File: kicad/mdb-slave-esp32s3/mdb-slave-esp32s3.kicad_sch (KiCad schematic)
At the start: 44 parts, among them J1 MDB_Connector, J2 USB_C_Receptacle_USB2.0_16P, J3 Conn_01x03_Pin, J8 Conn_01x04_Pin, Q7 MMBT3904, SW1 SW_Push, U1 TLP785, U3 ESP32-S3FH4R2, U4 TLP785, U5 LM2594HVM-3.3, Y1 Crystal_GND24

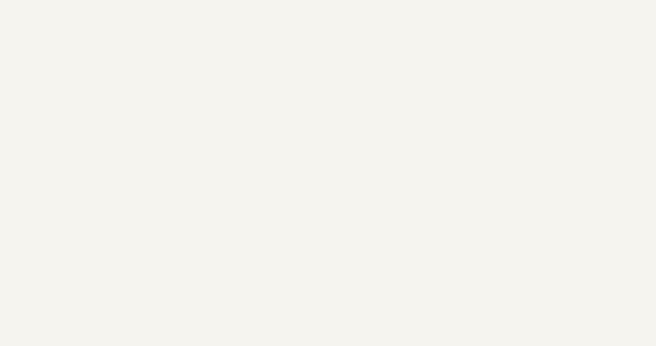
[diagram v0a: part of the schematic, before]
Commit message: small mounting hole
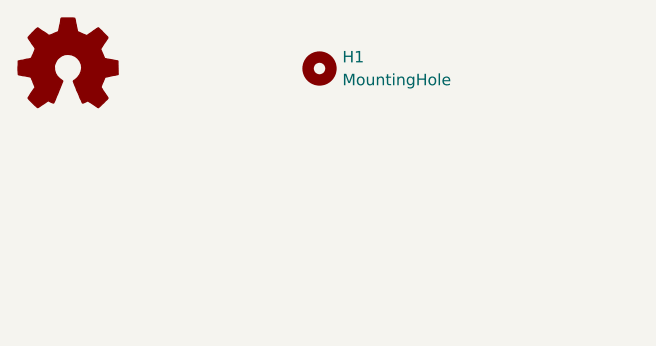
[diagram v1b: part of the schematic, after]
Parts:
- added H1: MountingHole, MountingHole:MountingHole_2.1mm, symbol Mechanical:MountingHole
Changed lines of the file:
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@@
+	)
+	(symbol
+		(lib_id "Graphic:Logo_Open_Hardware_Small")
+		(at 30.48 25.4 0)
+		(unit 1)
+		(exclude_from_sim yes)
+		(in_bom no)
+		(on_board no)
+		(dnp no)
+		(fields_autoplaced yes)
+		(property "Reference" "#SYM1"
+			(at 30.48 18.415 0)
+			(effects
+				(font
+					(size 1.27 1.27)
+				)
+				(hide yes)
+			)
+		)
+		(property "Value" "Logo_Open_Hardware_Small"
+			(at 30.48 31.115 0)
+			(effects
+				(font
+					(size 1.27 1.27)
+				)
+				(hide yes)
+			)
+		)
+		(property "Footprint" "Symbol:OSHW-Logo2_9.8x8mm_SilkScreen"
+			(at 30.48 25.4 0)
+			(effects
+				(font
+					(size 1.27 1.27)
+				)
+				(hide yes)
+			)
+		)
+		(property "Datasheet" "~"
+			(at 30.48 25.4 0)
+			(effects
+				(font
+					(size 1.27 1.27)
+				)
+				(hide yes)
+			)
+		)
+		(property "Description" "Open Hardware logo, small"
+			(at 30.48 25.4 0)
+			(effects
+				(font
+					(size 1.27 1.27)
+				)
+				(hide yes)
+			)
+		)
+		(instances
+			(project "mdb-slave-esp32s3"
+				(path "/95980b25-0707-441d-ba83-7f6c6e1d1aaa"
+					(reference "#SYM1")
+					(unit 1)
+				)
+			)
+		)
 	)
 	(symbol
@@
 					(unit 1)
 				)
+			)
+		)
+	)
+	(symbol
+		(lib_id "Mechanical:MountingHole")
+		(at 58.42 25.4 0)
+		(unit 1)
+		(exclude_from_sim no)
+		(in_bom no)
+		(on_board yes)
+		(dnp no)
+		(fields_autoplaced yes)
+		(property "Reference" "H1"
+			(at 60.96 24.1299 0)
+			(effects
+				(font
+					(size 1.27 1.27)
+				)
+				(justify left)
+			)
+		)
+		(property "Value" "MountingHole"
+			(at 60.96 26.6699 0)
+			(effects
+				(font
+					(size 1.27 1.27)
+				)
+				(justify left)
+			)
+		)
+		(property "Footprint" "MountingHole:MountingHole_2.1mm"
+			(at 58.42 25.4 0)
+			(effects
+				(font
+					(size 1.27 1.27)
+				)
+				(hide yes)
+			)
+		)
+		(property "Datasheet" "~"
+			(at 58.42 25.4 0)
+			(effects
+				(font
+					(size 1.27 1.27)
+				)
+				(hide yes)
+			)
+		)
+		(property "Description" "Mounting Hole without connection"
+			(at 58.42 25.4 0)
+			(effects
+				(font
+					(size 1.27 1.27)
+				)
+				(hide yes)
+			)
+		)
+		(property "Sim.Device" ""
+			(at 58.42 25.4 0)
+			(effects
+				(font
+					(size 1.27 1.27)
+				)
+				(hide yes)
+			)
+		)
+		(property "Sim.Pins" ""
+			(at 58.42 25.4 0)
+			(effects
+				(font
+					(size 1.27 1.27)
+				)
+				(hide yes)
+			)
+		)
+		(property "Sim.Type" ""
+			(at 58.42 25.4 0)
+			(effects
+				(font
+					(size 1.27 1.27)
+				)
+				(hide yes)
+			)
+		)
+		(instances
+			(project "mdb-slave-esp32s3"
+				(path "/95980b25-0707-441d-ba83-7f6c6e1d1aaa"
+					(reference "H1")
+					(unit 1)
+				)

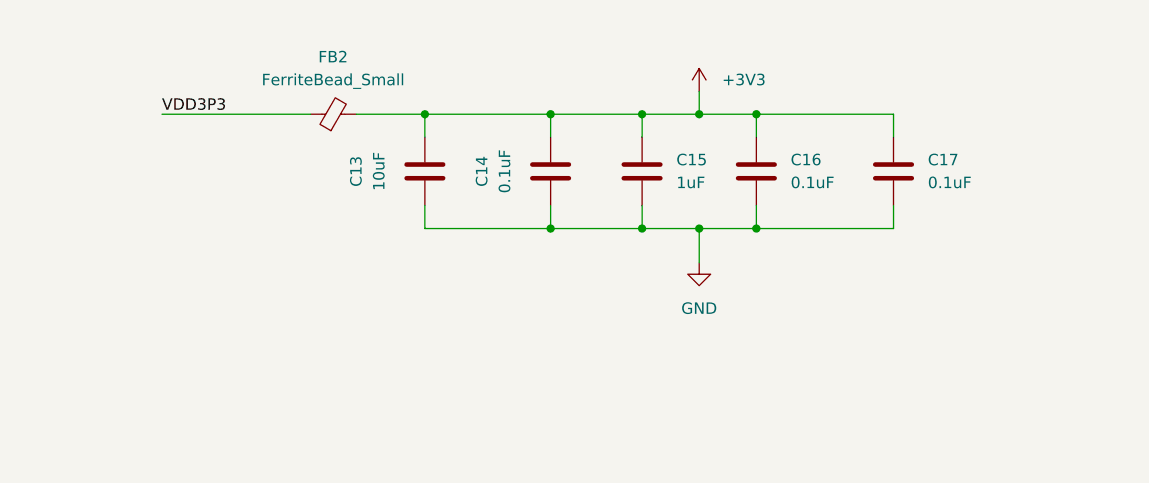
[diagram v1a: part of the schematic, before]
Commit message: moving capacitor 0.1uf to left ferrite bead
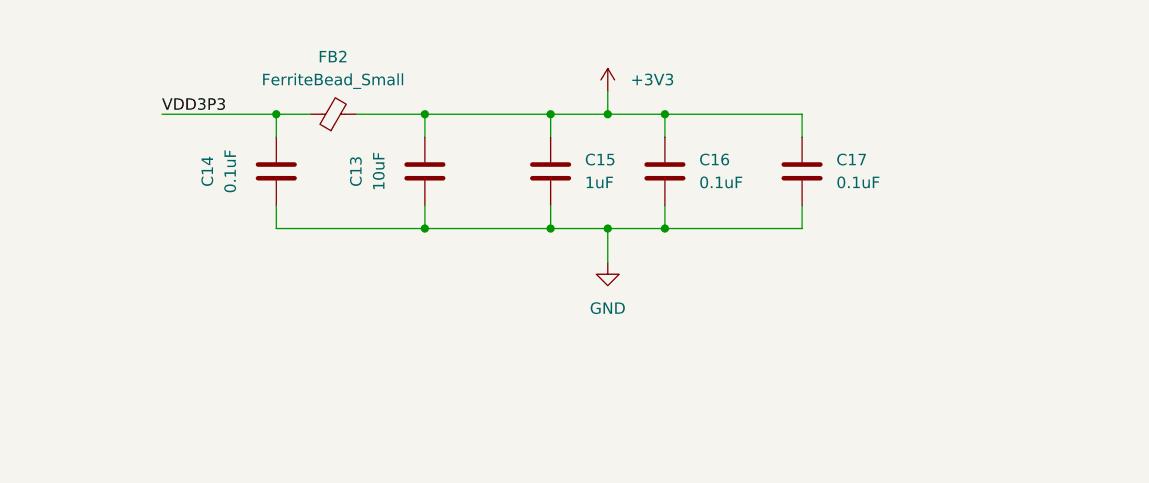
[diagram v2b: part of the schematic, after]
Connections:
- net +3V3: no longer C14.2
- net VDD3P3: now also C14.2
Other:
- moved on the sheet: C14, C15, C16, C17

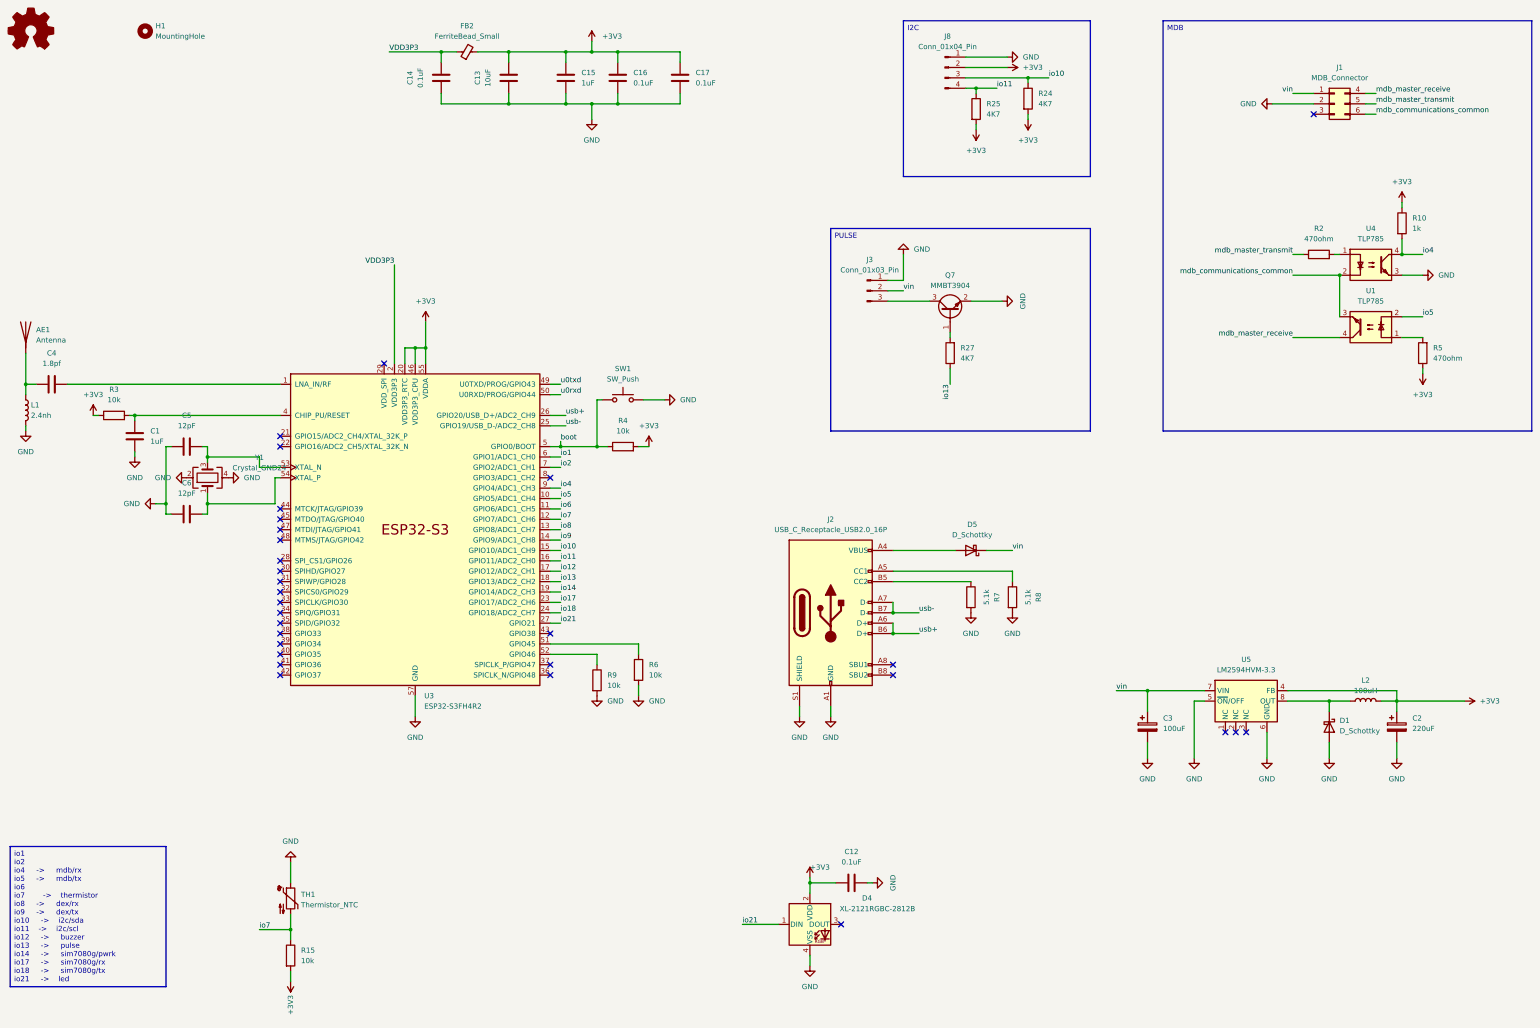
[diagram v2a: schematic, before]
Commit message: Including pulse rx (#62)
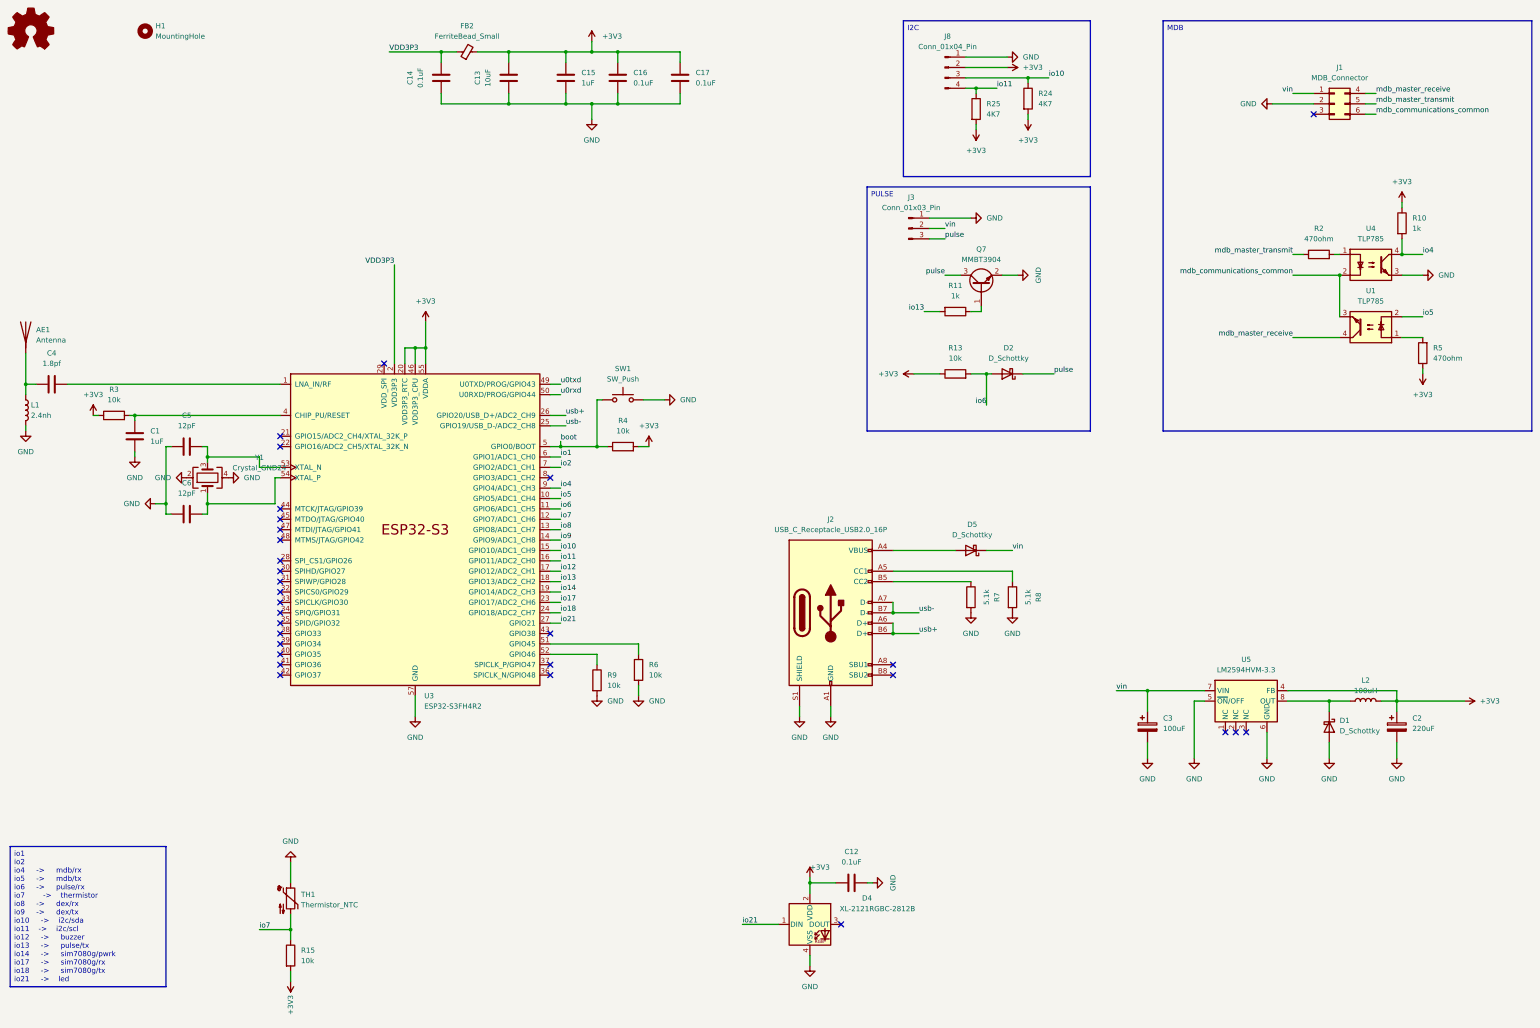
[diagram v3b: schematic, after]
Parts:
- removed R27: 4K7, Resistor_SMD:R_0603_1608Metric, symbol Device:R
- added D2: D_Schottky, Diode_SMD:D_SOD-123, symbol Device:D_Schottky
- added R11: 1k, Resistor_SMD:R_0603_1608Metric, symbol Device:R
- added R13: 10k, Resistor_SMD:R_0603_1608Metric, symbol Device:R
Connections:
- net +3V3: now also R13.1
- net io13: now also R11.2
- net io6: now also D2.2 (A), R13.2
- net at Q7.1 (B): now also R11.1
- net pulse: now reaches J3.3 (Pin_3), Q7.3 (C)
- net pulse: now also D2.1 (K)
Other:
- moved on the sheet: J3, Q7
